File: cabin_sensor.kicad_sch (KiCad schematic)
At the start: 6 parts, among them J5 Внутр. коннектор вентилятора 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, Q2 AO3400

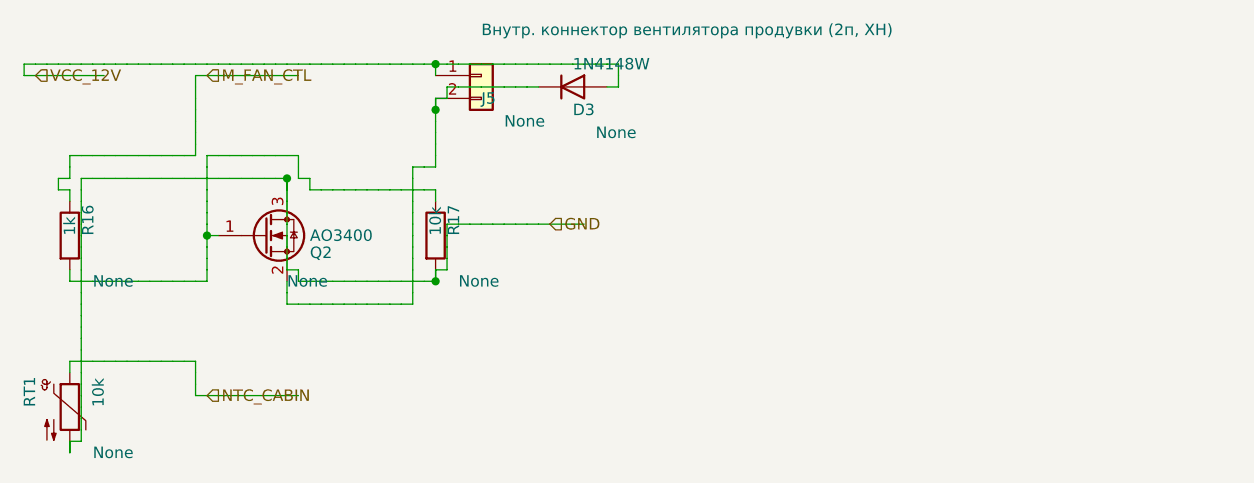
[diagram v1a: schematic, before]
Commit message: fix router map cell no more mark for pins
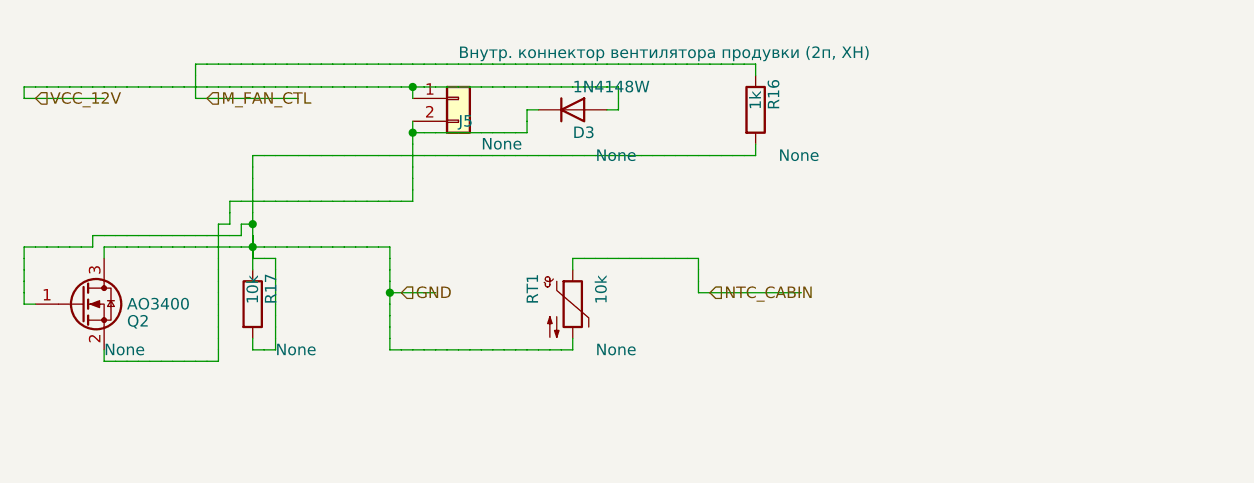
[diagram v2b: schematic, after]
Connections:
- net VCC_12V is gone; now on net M_FAN_CTL: D3.2 (A), J5.1 (Pin_1)
- net GND: no longer RT1.1
- new net NTC_CABIN: RT1.1

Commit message: fix writer
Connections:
- net GND: no longer D3.1 (K), J5.2 (Pin_2), Q2.2 (S)
- net M_FAN_CTL: no longer D3.2 (A), J5.1 (Pin_1)
- new net: D3.1 (K), J5.2 (Pin_2), Q2.2 (S)
- new net VCC_12V: D3.2 (A), J5.1 (Pin_1)

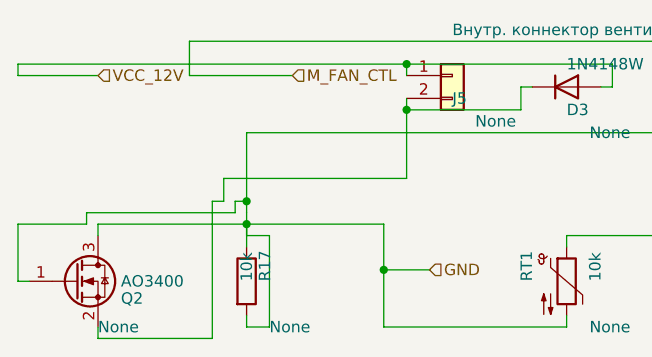
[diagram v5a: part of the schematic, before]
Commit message: реализована 2я занятость клетки
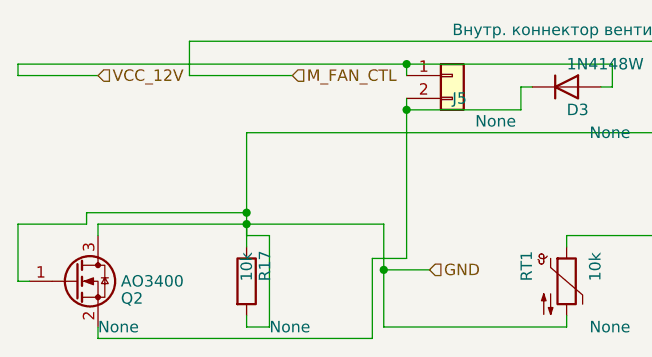
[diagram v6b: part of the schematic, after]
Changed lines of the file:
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@@
 		(instances
 			(project "Untitled"
-				(path "/9595c01b-4b9d-4b6b-a2c4-870fe7ef478e"
+				(path "/e62f4b3a-36c9-4e33-a73c-6729ffa31e85"
 					(reference "D3")
 					(unit 1)
@@
 		(instances
 			(project "Untitled"
-				(path "/9595c01b-4b9d-4b6b-a2c4-870fe7ef478e"
+				(path "/e62f4b3a-36c9-4e33-a73c-6729ffa31e85"
 					(reference "J5")
 					(unit 1)
@@
 		(instances
 			(project "Untitled"
-				(path "/9595c01b-4b9d-4b6b-a2c4-870fe7ef478e"
+				(path "/e62f4b3a-36c9-4e33-a73c-6729ffa31e85"
 					(reference "Q2")
 					(unit 1)
@@
 		(instances
 			(project "Untitled"
-				(path "/9595c01b-4b9d-4b6b-a2c4-870fe7ef478e"
+				(path "/e62f4b3a-36c9-4e33-a73c-6729ffa31e85"
 					(reference "R16")
 					(unit 1)
@@
 		(instances
 			(project "Untitled"
-				(path "/9595c01b-4b9d-4b6b-a2c4-870fe7ef478e"
+				(path "/e62f4b3a-36c9-4e33-a73c-6729ffa31e85"
 					(reference "R17")
 					(unit 1)
@@
 		(instances
 			(project "Untitled"
-				(path "/9595c01b-4b9d-4b6b-a2c4-870fe7ef478e"
+				(path "/e62f4b3a-36c9-4e33-a73c-6729ffa31e85"
 					(reference "RT1")
 					(unit 1)
@@
 	(wire
 		(pts
-			(xy 10.16 21.59) (xy 26.67 21.59)
-		)
-		(stroke
-			(width 0)
-			(type default)
-		)
-	)
-	(wire
-		(pts
-			(xy 26.67 21.59) (xy 26.67 20.32)
-		)
-		(stroke
-			(width 0)
-			(type default)
-		)
-	)
-	(wire
-		(pts
-			(xy 26.67 20.32) (xy 27.94 20.32)
-		)
-		(stroke
-			(width 0)
-			(type default)
-		)
-	)
-	(wire
-		(pts
-			(xy 27.94 20.32) (xy 27.94 21.59)
+			(xy 10.16 21.59) (xy 27.94 21.59)
 		)
 		(stroke
@@
 	(wire
 		(pts
-			(xy 27.94 12.7) (xy 27.94 20.32)
+			(xy 27.94 12.7) (xy 27.94 21.59)
 		)
 		(stroke
@@
 	(wire
 		(pts
-			(xy 11.43 35.56) (xy 24.13 35.56)
-		)
-		(stroke
-			(width 0)
-			(type default)
-		)
-	)
-	(wire
-		(pts
-			(xy 24.13 35.56) (xy 24.13 20.32)
-		)
-		(stroke
-			(width 0)
-			(type default)
-		)
-	)
-	(wire
-		(pts
-			(xy 24.13 20.32) (xy 25.4 20.32)
-		)
-		(stroke
-			(width 0)
-			(type default)
-		)
-	)
-	(wire
-		(pts
-			(xy 25.4 20.32) (xy 25.4 17.78)
-		)
-		(stroke
-			(width 0)
-			(type default)
-		)
-	)
-	(wire
-		(pts
-			(xy 25.4 17.78) (xy 45.72 17.78)
-		)
-		(stroke
-			(width 0)
-			(type default)
-		)
-	)
-	(wire
-		(pts
-			(xy 45.72 17.78) (xy 45.72 10.16)
+			(xy 11.43 35.56) (xy 41.91 35.56)
+		)
+		(stroke
+			(width 0)
+			(type default)
+		)
+	)
+	(wire
+		(pts
+			(xy 41.91 35.56) (xy 41.91 26.67)
+		)
+		(stroke
+			(width 0)
+			(type default)
+		)
+	)
+	(wire
+		(pts
+			(xy 41.91 26.67) (xy 45.72 26.67)
+		)
+		(stroke
+			(width 0)
+			(type default)
+		)
+	)
+	(wire
+		(pts
+			(xy 45.72 26.67) (xy 45.72 10.16)
 		)
 		(stroke
@@
 	)
 	(junction
-		(at 27.94 20.32)
+		(at 27.94 21.59)
 		(diameter 0)
 		(color 0 0 0 0)

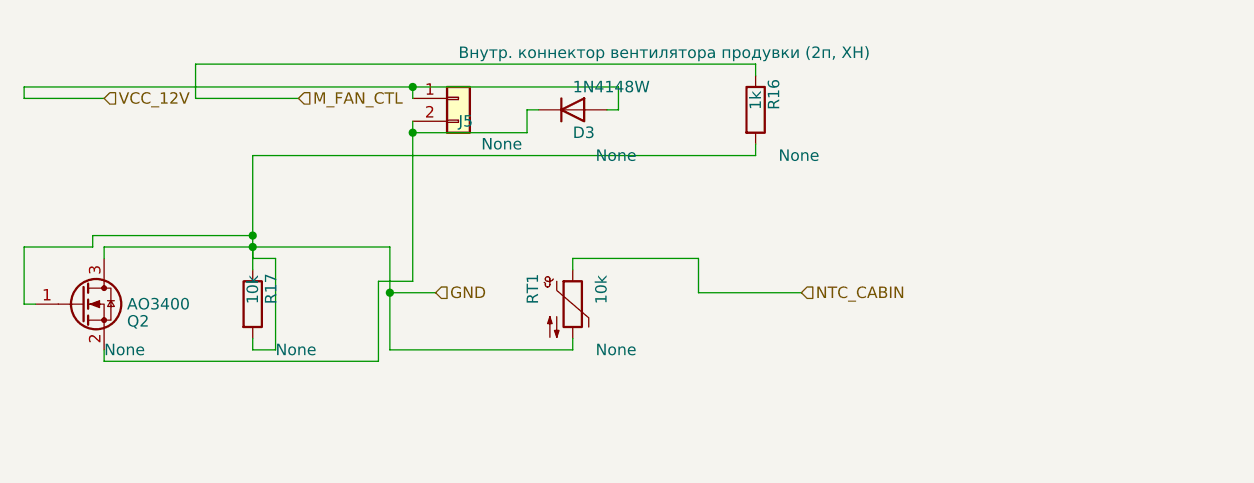
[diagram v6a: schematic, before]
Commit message: фильтр клеток для Т если там пересечение
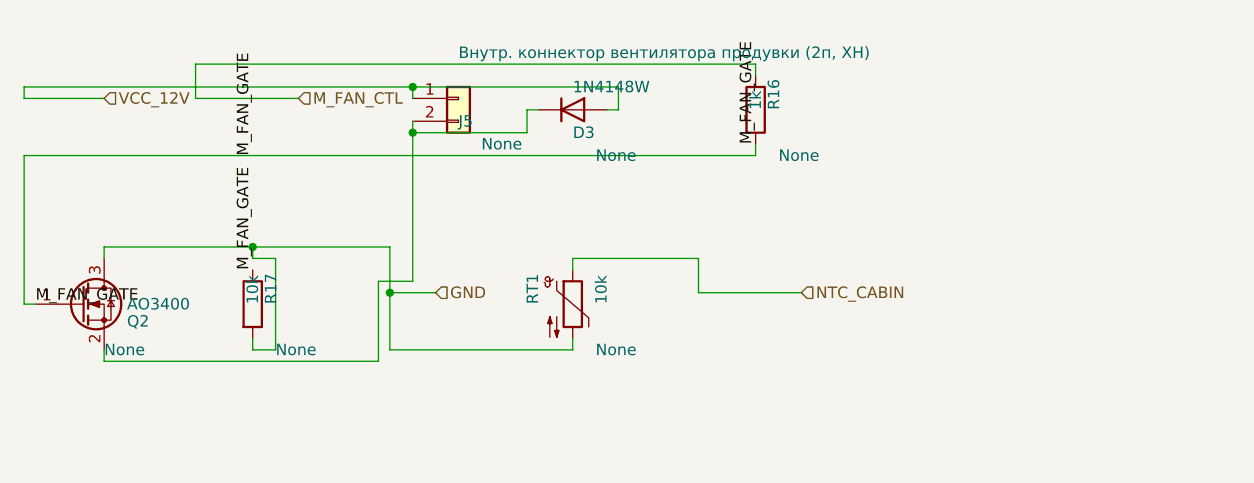
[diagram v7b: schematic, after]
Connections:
- net GND: no longer Q2.1 (G), R16.2, R17.1
- new net M_FAN_GATE: Q2.1 (G), R16.2, R17.1
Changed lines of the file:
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@@
 		(instances
 			(project "Untitled"
-				(path "/e62f4b3a-36c9-4e33-a73c-6729ffa31e85"
+				(path "/bec90f06-7e14-4a30-a332-b1f9f79f2d38"
 					(reference "D3")
 					(unit 1)
@@
 		(instances
 			(project "Untitled"
-				(path "/e62f4b3a-36c9-4e33-a73c-6729ffa31e85"
+				(path "/bec90f06-7e14-4a30-a332-b1f9f79f2d38"
 					(reference "J5")
 					(unit 1)
@@
 		(instances
 			(project "Untitled"
-				(path "/e62f4b3a-36c9-4e33-a73c-6729ffa31e85"
+				(path "/bec90f06-7e14-4a30-a332-b1f9f79f2d38"
 					(reference "Q2")
 					(unit 1)
@@
 		(instances
 			(project "Untitled"
-				(path "/e62f4b3a-36c9-4e33-a73c-6729ffa31e85"
+				(path "/bec90f06-7e14-4a30-a332-b1f9f79f2d38"
 					(reference "R16")
 					(unit 1)
@@
 		(instances
 			(project "Untitled"
-				(path "/e62f4b3a-36c9-4e33-a73c-6729ffa31e85"
+				(path "/bec90f06-7e14-4a30-a332-b1f9f79f2d38"
 					(reference "R17")
 					(unit 1)
@@
 		(instances
 			(project "Untitled"
-				(path "/e62f4b3a-36c9-4e33-a73c-6729ffa31e85"
+				(path "/bec90f06-7e14-4a30-a332-b1f9f79f2d38"
 					(reference "RT1")
 					(unit 1)
@@
 	(wire
 		(pts
-			(xy 3.81 29.21) (xy 2.54 29.21)
-		)
-		(stroke
-			(width 0)
-			(type default)
-		)
-	)
-	(wire
-		(pts
-			(xy 2.54 29.21) (xy 2.54 22.86)
-		)
-		(stroke
-			(width 0)
-			(type default)
-		)
-	)
-	(wire
-		(pts
-			(xy 2.54 22.86) (xy 10.16 22.86)
-		)
-		(stroke
-			(width 0)
-			(type default)
-		)
-	)
-	(wire
-		(pts
-			(xy 10.16 22.86) (xy 10.16 21.59)
-		)
-		(stroke
-			(width 0)
-			(type default)
-		)
-	)
-	(wire
-		(pts
-			(xy 10.16 21.59) (xy 27.94 21.59)
-		)
-		(stroke
-			(width 0)
-			(type default)
-		)
-	)
-	(wire
-		(pts
-			(xy 27.94 21.59) (xy 27.94 25.4)
-		)
-		(stroke
-			(width 0)
-			(type default)
-		)
-	)
-	(wire
-		(pts
 			(xy 83.82 11.43) (xy 83.82 12.7)
 		)
@@
 	(wire
 		(pts
-			(xy 83.82 12.7) (xy 27.94 12.7)
-		)
-		(stroke
-			(width 0)
-			(type default)
-		)
-	)
-	(wire
-		(pts
-			(xy 27.94 12.7) (xy 27.94 21.59)
+			(xy 83.82 12.7) (xy 2.54 12.7)
+		)
+		(stroke
+			(width 0)
+			(type default)
+		)
+	)
+	(wire
+		(pts
+			(xy 2.54 12.7) (xy 2.54 29.21)
+		)
+		(stroke
+			(width 0)
+			(type default)
+		)
+	)
+	(wire
+		(pts
+			(xy 2.54 29.21) (xy 3.81 29.21)
 		)
 		(stroke
@@
 	)
 	(junction
-		(at 27.94 21.59)
-		(diameter 0)
-		(color 0 0 0 0)
-	)
-	(junction
 		(at 45.72 10.16)
 		(diameter 0)
 		(color 0 0 0 0)
 	)
+	(label "M_FAN_GATE"
+		(at 3.81 29.21 180)
+		(effects
+			(font
+				(size 1.27 1.27)
+			)
+			(justify left bottom)
+		)
+	)
+	(label "M_FAN_GATE"
+		(at 27.94 25.4 90)
+		(effects
+			(font
+				(size 1.27 1.27)
+			)
+			(justify left bottom)
+		)
+	)
+	(label "M_FAN_GATE"
+		(at 83.82 11.43 270)
+		(effects
+			(font
+				(size 1.27 1.27)
+			)
+			(justify left bottom)
+		)
+	)
+	(label "M_FAN_GATE"
+		(at 27.94 12.7 90)
+		(effects
+			(font
+				(size 1.27 1.27)
+			)
+			(justify left bottom)
+		)
+	)
 	(hierarchical_label "VCC_12V"

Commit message: fic placer for small schemes
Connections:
- net SENS_FAN_SW: now reaches D3.1 (K), J5.2 (Pin_2), Q2.2 (S)
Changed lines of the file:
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@@
 		(instances
 			(project "Untitled"
-				(path "/bec90f06-7e14-4a30-a332-b1f9f79f2d38"
+				(path "/d2d9c845-ec0d-449c-abb0-f5fdcc359b62"
 					(reference "D3")
 					(unit 1)
@@
 		(instances
 			(project "Untitled"
-				(path "/bec90f06-7e14-4a30-a332-b1f9f79f2d38"
+				(path "/d2d9c845-ec0d-449c-abb0-f5fdcc359b62"
 					(reference "J5")
 					(unit 1)
@@
 		(instances
 			(project "Untitled"
-				(path "/bec90f06-7e14-4a30-a332-b1f9f79f2d38"
+				(path "/d2d9c845-ec0d-449c-abb0-f5fdcc359b62"
 					(reference "Q2")
 					(unit 1)
@@
 		(instances
 			(project "Untitled"
-				(path "/bec90f06-7e14-4a30-a332-b1f9f79f2d38"
+				(path "/d2d9c845-ec0d-449c-abb0-f5fdcc359b62"
 					(reference "R16")
 					(unit 1)
@@
 		(instances
 			(project "Untitled"
-				(path "/bec90f06-7e14-4a30-a332-b1f9f79f2d38"
+				(path "/d2d9c845-ec0d-449c-abb0-f5fdcc359b62"
 					(reference "R17")
 					(unit 1)
@@
 		(instances
 			(project "Untitled"
-				(path "/bec90f06-7e14-4a30-a332-b1f9f79f2d38"
+				(path "/d2d9c845-ec0d-449c-abb0-f5fdcc359b62"
 					(reference "RT1")
 					(unit 1)
@@
 		(effects
 			(font
+				(size 1.27 1.27)
+			)
+			(justify left bottom)
+		)
+	)
+	(label "SENS_FAN_SW"
+		(at 26.67 35.56 270)
+		(effects
+			(font
